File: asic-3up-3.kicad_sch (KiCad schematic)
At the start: 77 parts, among them J10 Conn_01x01, J11 Conn_01x01, U66 MCP1824T-1202E/OT, U67 MCP1824T-1202E/OT, U68 MCP1824T-1202E/OT, U69 MCP1824T-0802E, U70 MCP1824T-0802E, U71 MCP1824T-0802E, U72 BM1362AC_MODE1, U73 BM1362AC_MODE0, U74 BM1362AC_MODE1

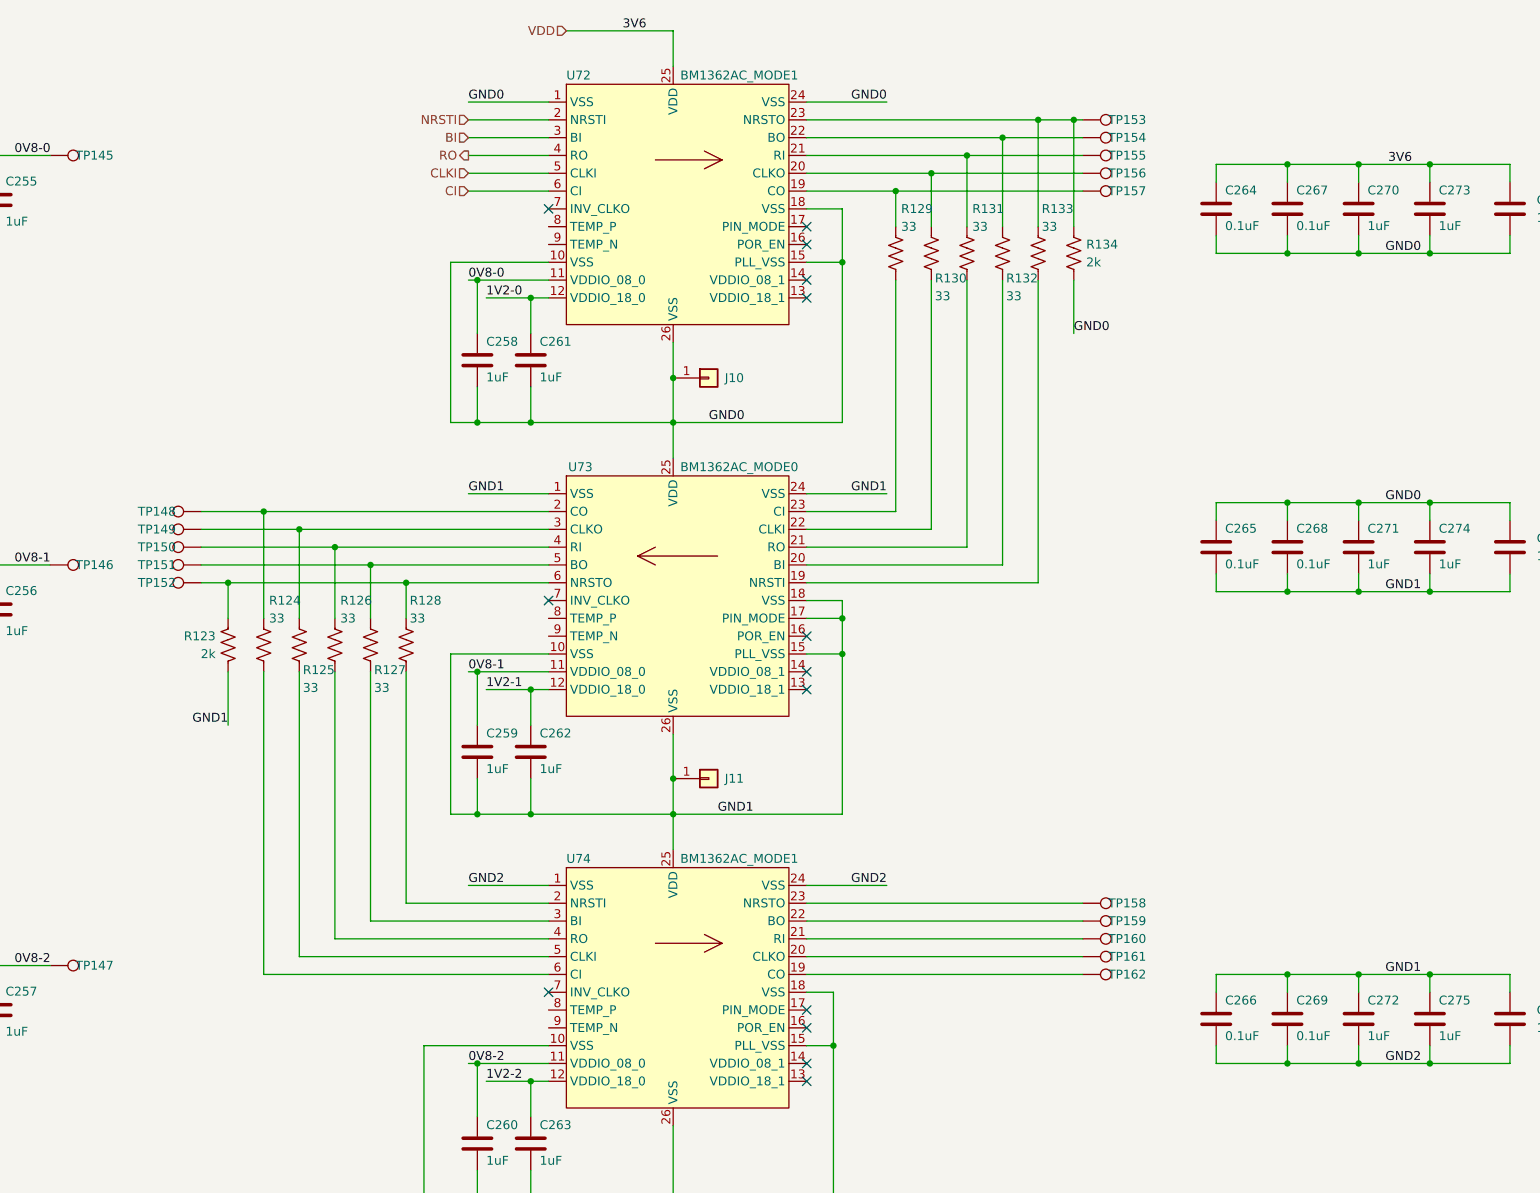
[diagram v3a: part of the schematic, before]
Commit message: so much placing. added mask and paste opening on ASIC footprints. added a pad for a rear heatsink
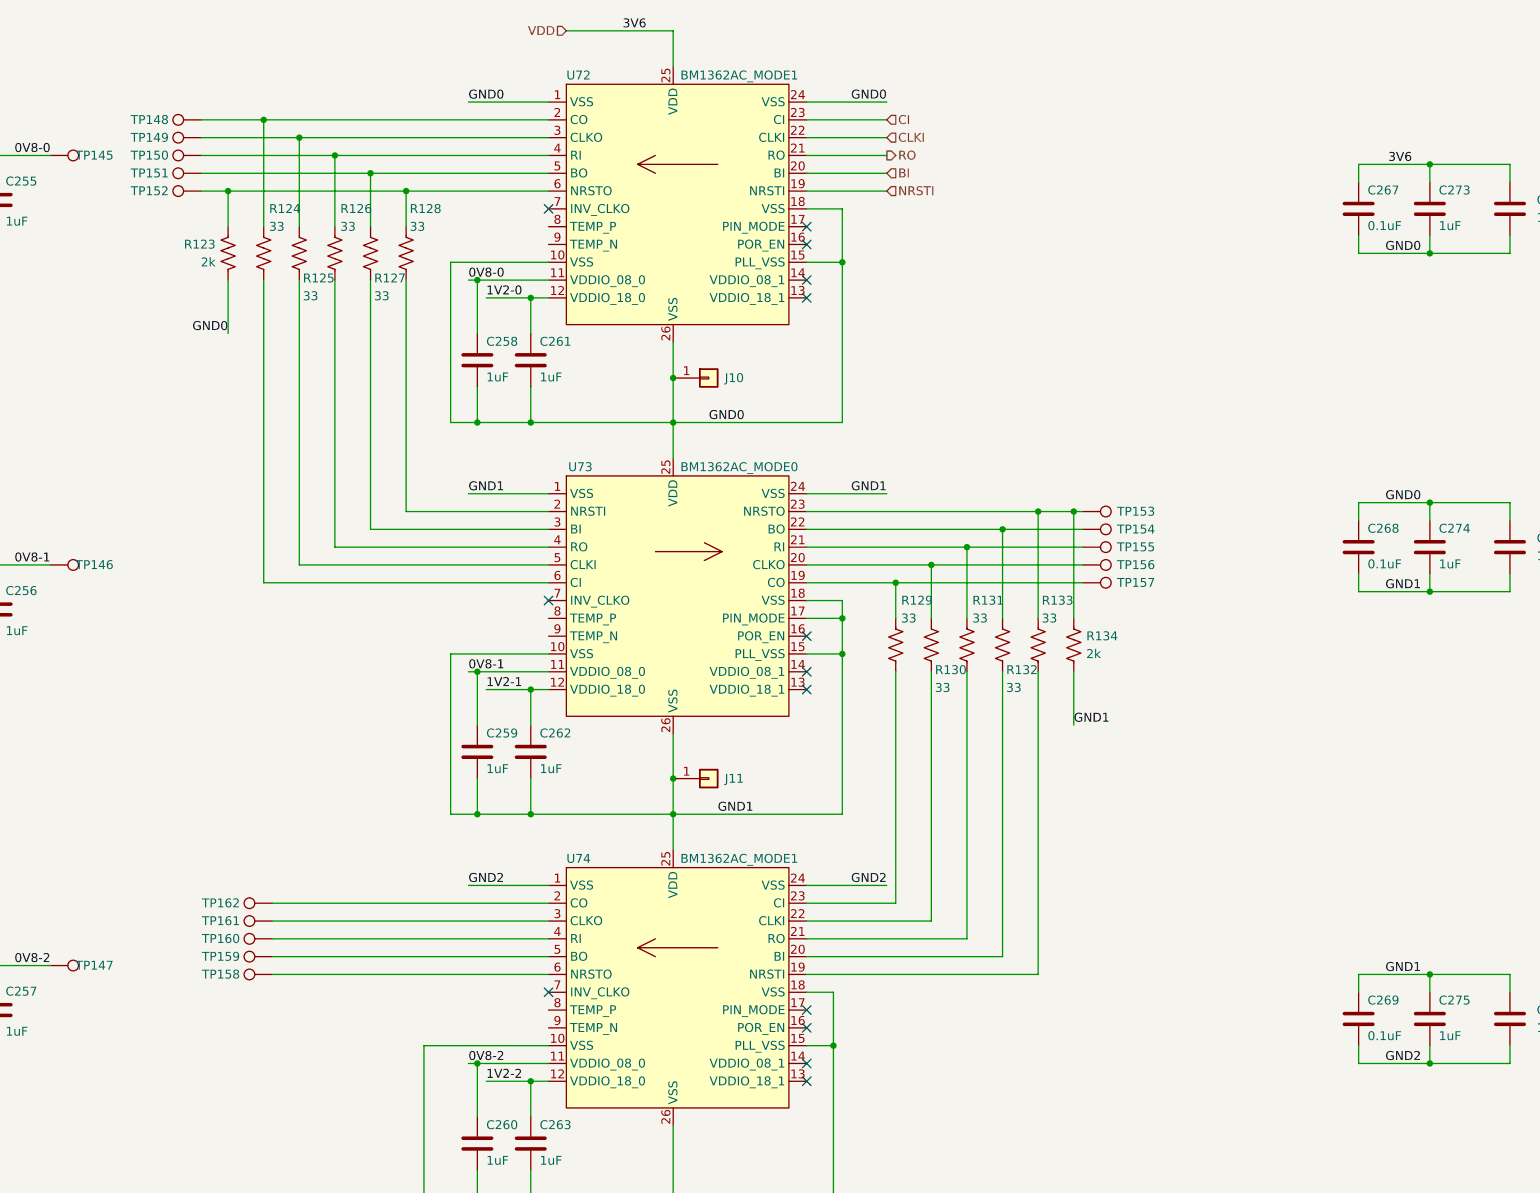
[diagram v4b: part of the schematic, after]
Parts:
- removed C264, C265, C266: 0.1uF, Capacitor_SMD:C_0402_1005Metric, symbol Device:C
- removed C270, C271, C272: 1uF, Capacitor_SMD:C_0402_1005Metric, symbol Device:C
- U72, U74: symbol emberone:BM1362AC_MODE1 -> emberone:BM1362AC_MODE0
- U73: symbol emberone:BM1362AC_MODE0 -> emberone:BM1362AC_MODE1
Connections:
- net BI: now also U72.20 (BI); no longer U72.3 (BI)
- net CI: now also U72.23 (CI); no longer U72.6 (CI)
- net CLKI: now also U72.22 (CLKI); no longer U72.5 (CLKI)
- net GND0: now also R123.2; no longer R134.2
- net GND1: now also R134.2; no longer R123.2
- net NRSTI: now also U72.19 (NRSTI); no longer U72.2 (NRSTI)
- net RO: now also U72.21 (RO); no longer U72.4 (RO)
- net at R133.1, R134.1, TP153.1: now also U73.23 (NRSTO); no longer U72.23 (NRSTO)
- net at R124.1, TP148.1: now also U72.2 (CO); no longer U73.2 (CO)
- net at R130.1, TP156.1: now also U73.20 (CLKO); no longer U72.20 (CLKO)
- net at R130.2: now also U74.22 (CLKI); no longer U73.22 (CLKI)
- net at R129.1, TP157.1: now also U73.19 (CO); no longer U72.19 (CO)
- net at R133.2: now also U74.19 (NRSTI); no longer U73.19 (NRSTI)
- net at TP158.1: now also U74.6 (NRSTO); no longer U74.23 (NRSTO)
- net at R123.1, R128.1, TP152.1: now also U72.6 (NRSTO); no longer U73.6 (NRSTO)
- net at R128.2: now also U73.2 (NRSTI); no longer U74.2 (NRSTI)
- net at R132.1, TP154.1: now also U73.22 (BO); no longer U72.22 (BO)
- net at R131.1, TP155.1: now also U73.21 (RI); no longer U72.21 (RI)
- net at TP160.1: now also U74.4 (RI); no longer U74.21 (RI)
- net at TP161.1: now also U74.3 (CLKO); no longer U74.20 (CLKO)
- net at TP159.1: now also U74.5 (BO); no longer U74.22 (BO)
- net at R132.2: now also U74.20 (BI); no longer U73.20 (BI)
- net at R131.2: now also U74.21 (RO); no longer U73.21 (RO)
- net at R129.2: now also U74.23 (CI); no longer U73.23 (CI)
- net at R125.1, TP149.1: now also U72.3 (CLKO); no longer U73.3 (CLKO)
- net at R126.1, TP150.1: now also U72.4 (RI); no longer U73.4 (RI)
- net at R127.1, TP151.1: now also U72.5 (BO); no longer U73.5 (BO)
- net at TP162.1: now also U74.2 (CO); no longer U74.19 (CO)
- net at R127.2: now also U73.3 (BI); no longer U74.3 (BI)
- net at R126.2: now also U73.4 (RO); no longer U74.4 (RO)
- net at R125.2: now also U73.5 (CLKI); no longer U74.5 (CLKI)
- net at R124.2: now also U73.6 (CI); no longer U74.6 (CI)
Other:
- moved on the sheet: C267, C268, C269, R123, R124, R125, R126, R127, R128, R129, R130, R131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

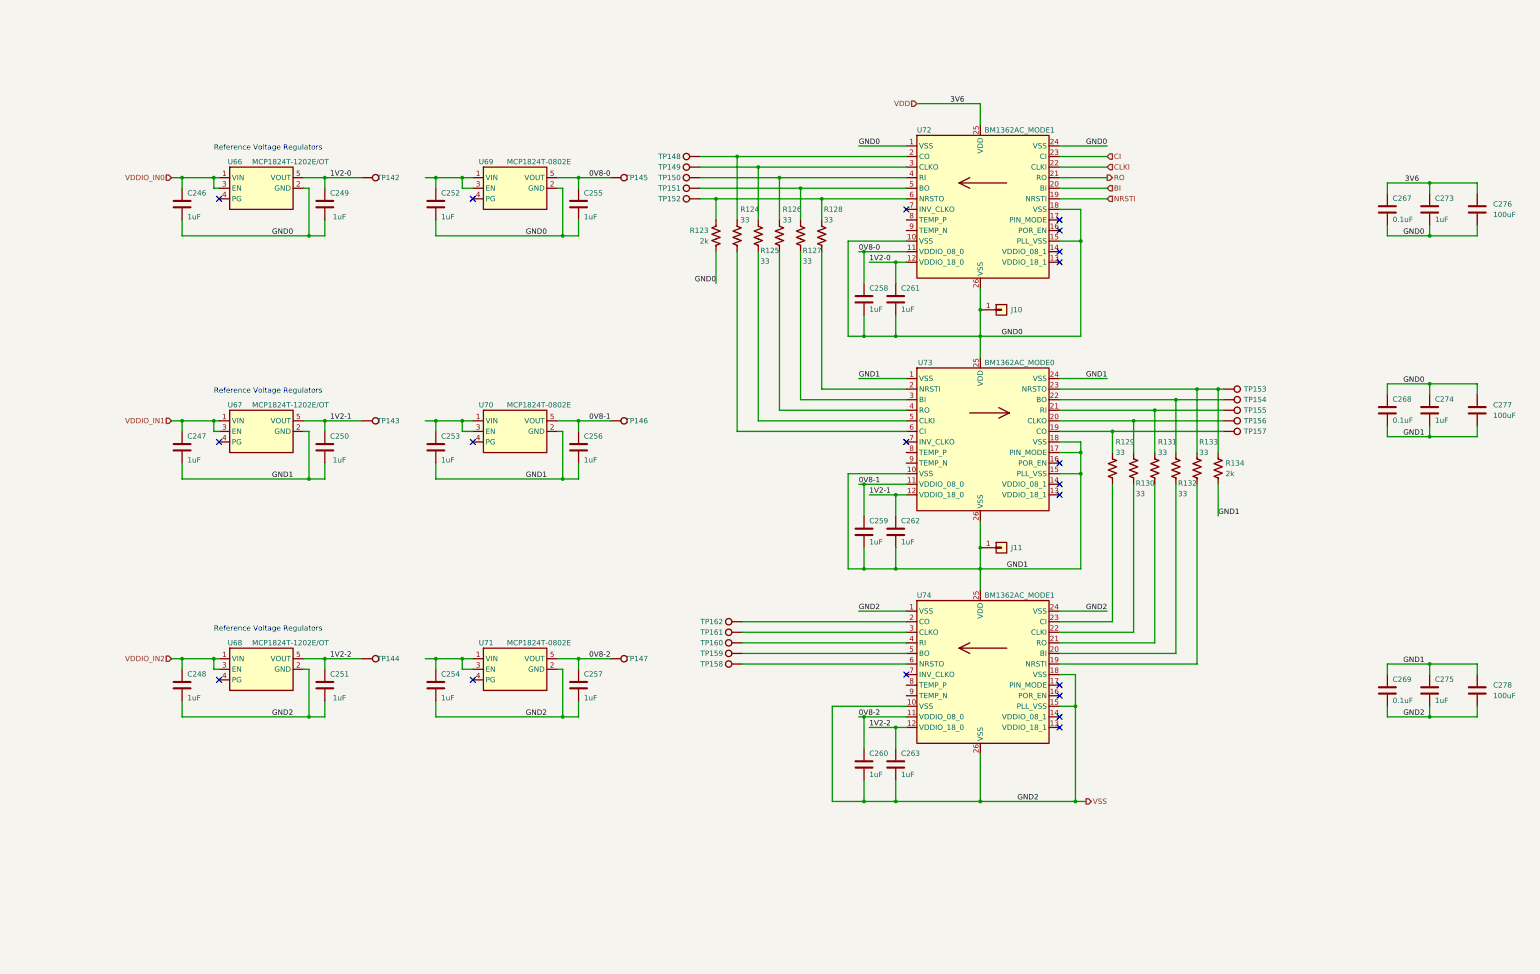
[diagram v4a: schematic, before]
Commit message: forgot that data needs to start with the ASIC that has GND at system GND... reversed everything
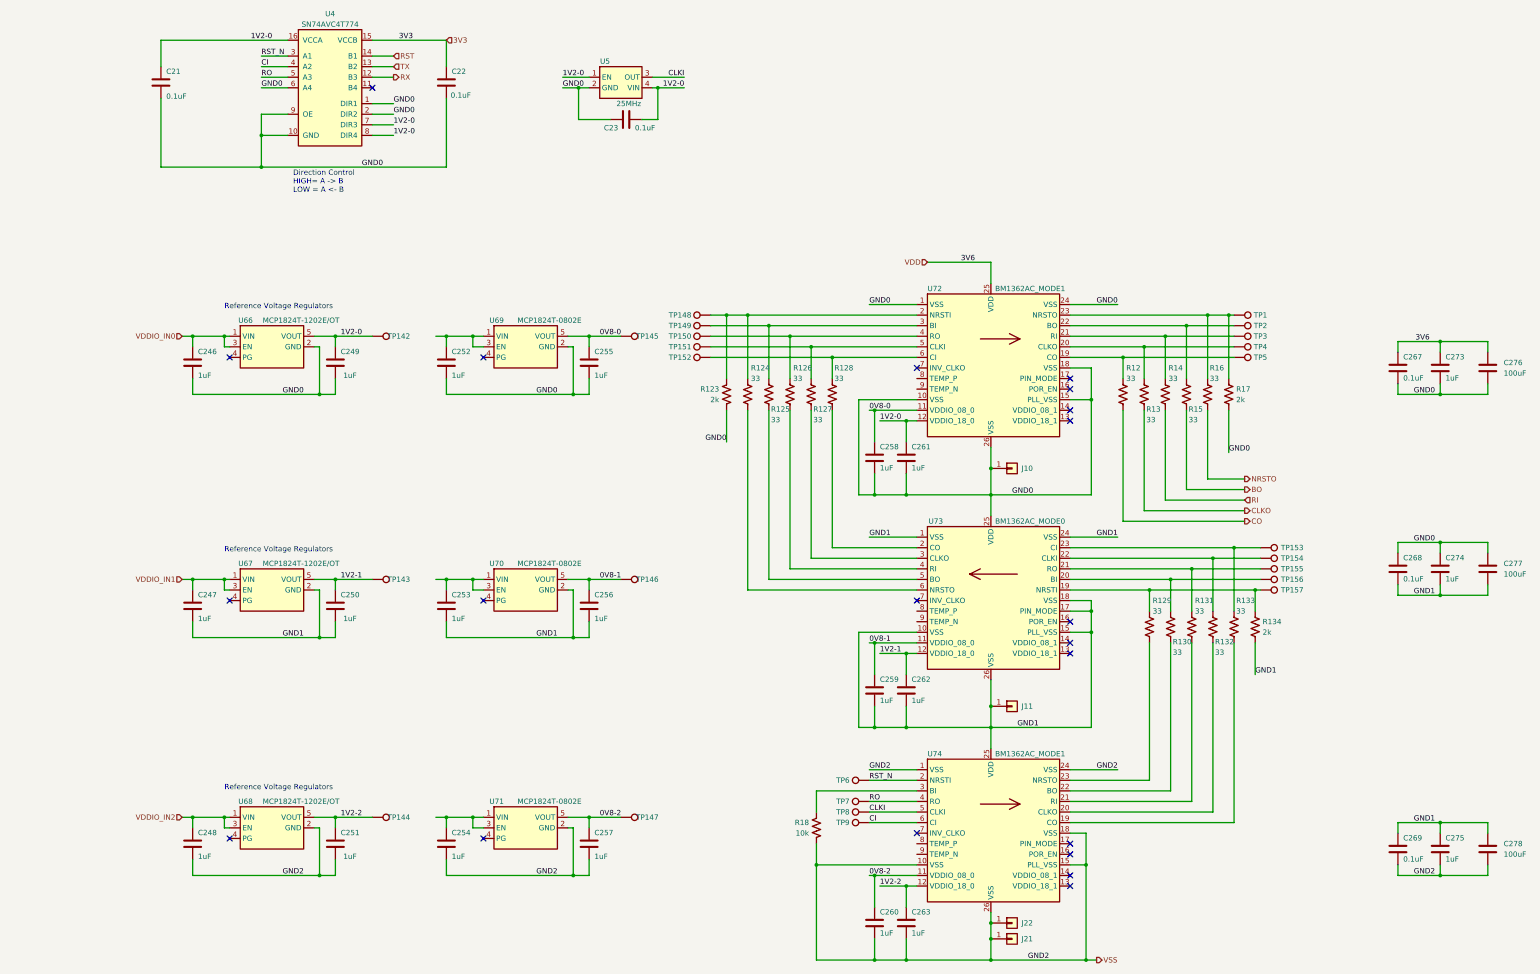
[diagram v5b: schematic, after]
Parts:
- removed TP158, TP159, TP160, TP161, TP162: TestPoint, TestPoint:TestPoint_Pad_D1.5mm, symbol Connector:TestPoint
- added C21, C22, C23: 0.1uF, Capacitor_SMD:C_0402_1005Metric, symbol Device:C
- added J21: Conn_01x01, emberone:5x9_powertab, symbol Connector_Generic:Conn_01x01
- added J22: Conn_01x01, emberone:14x9_powertab_L, symbol Connector_Generic:Conn_01x01
- added R12, R13, R14, R15, R16: 33, Resistor_SMD:R_0402_1005Metric, symbol Device:R_US
- added R17: 2k, Resistor_SMD:R_0402_1005Metric, symbol Device:R_US
- added R18: 10k, Resistor_SMD:R_0402_1005Metric, symbol Device:R_US
- added TP1, TP2, TP3, TP4, TP5, TP6, TP7, TP8, TP9: TestPoint, TestPoint:TestPoint_Pad_D1.5mm, symbol Connector:TestPoint
- added U4: SN74AVC4T774, Package_SO:TSSOP-16_4.4x5mm_P0.65mm, symbol bitaxe:SN74AVC4T774
- added U5: 25MHz, bitaxe:SMD3225-4P, symbol bitaxe:oscillator
- U72, U74: symbol emberone:BM1362AC_MODE0 -> emberone:BM1362AC_MODE1
- U73: symbol emberone:BM1362AC_MODE1 -> emberone:BM1362AC_MODE0
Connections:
- net 1V2-0: now also C21.1, C23.2, U4.16 (VCCA), U4.7 (DIR3), U4.8 (DIR4), U5.1 (EN), U5.4 (VIN)
- net CI: now also U74.6 (CI), TP9.1, U4.4 (A2); no longer U72.23 (CI)
- net CLKI: now also U74.5 (CLKI), TP8.1, U5.3 (OUT); no longer U72.22 (CLKI)
- net GND0: now also C21.2, C22.2, C23.1, R17.2, U4.1 (DIR1), U4.10 (GND), U4.2 (DIR2), U4.6 (A4), U4.9 (OE), U5.2 (GND)
- net RO: now also U74.4 (RO), TP7.1, U4.5 (A3); no longer U72.21 (RO)
- net VSS: now also J21.1 (Pin_1), J22.1 (Pin_1), R18.2
- net at R133.1, TP153.1, U73.23 (CI): no longer R134.1
- net at R124.1, TP148.1, U72.2 (NRSTI): now also R123.1
- net at R129.1, TP157.1, U73.19 (NRSTI): now also R134.1
- net at R128.1, TP152.1, U72.6 (CI): no longer R123.1
- net at U74.3 (BI): now also R18.1
- net RST_N: now reaches U74.2 (NRSTI)
- net RST_N: now also TP6.1, U4.3 (A1)
- net BI: no longer names the net of U72.20 (CLKO)
- net BI: now also R13.1, TP4.1
- net NRSTI: no longer names the net of U72.19 (CO)
- net NRSTI: now also R12.1, TP5.1
- new net: R14.1, TP3.1, U72.21 (RI)
- new net: R16.1, R17.1, TP1.1, U72.23 (NRSTO)
- new net: R15.1, TP2.1, U72.22 (BO)
- new net 3V3: C22.1, U4.15 (VCCB)
- new net BO: R15.2
- new net CLKO: R13.2
- new net CO: R12.2
- new net NRSTO: R16.2
- new net RI: R14.2
- new net RST: U4.14 (B1)
- new net RX: U4.12 (B3)
- new net TX: U4.13 (B2)
- no-connect marks 20 -> 21
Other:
- note added: "Direction Control HIGH= A -> B LOW = A <- B"
- moved on the sheet: C246, C247, C248, C249, C250, C251, C252, C253, C254, C255, C256, C257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

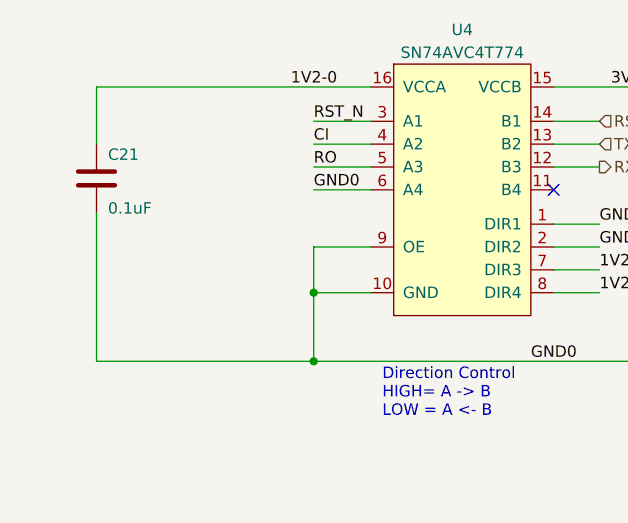
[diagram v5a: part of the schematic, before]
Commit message: added the heatsink mounting holes
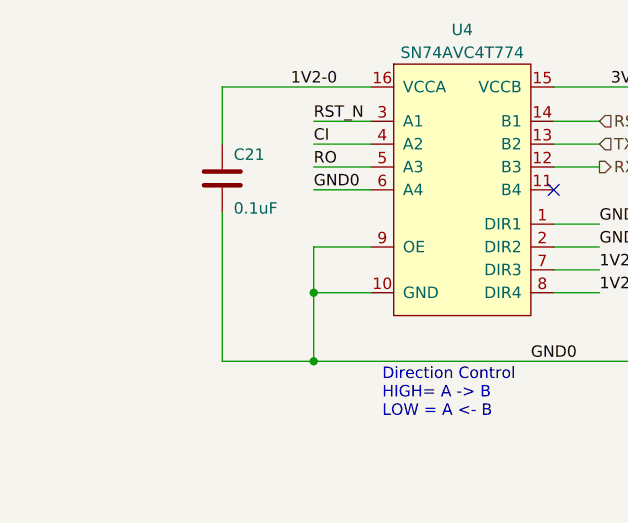
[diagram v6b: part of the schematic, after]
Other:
- moved on the sheet: C21
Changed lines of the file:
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@@
 	(wire
 		(pts
-			(xy 49.53 34.29) (xy 49.53 40.64)
+			(xy 63.5 34.29) (xy 63.5 40.64)
 		)
 		(stroke
@@
 	(wire
 		(pts
-			(xy 49.53 64.77) (xy 73.66 64.77)
+			(xy 63.5 64.77) (xy 73.66 64.77)
 		)
 		(stroke
@@
 	(wire
 		(pts
-			(xy 49.53 48.26) (xy 49.53 64.77)
+			(xy 63.5 48.26) (xy 63.5 64.77)
 		)
 		(stroke
@@
 	(wire
 		(pts
-			(xy 49.53 34.29) (xy 80.01 34.29)
+			(xy 63.5 34.29) (xy 80.01 34.29)
 		)
 		(stroke
@@
 	(symbol
 		(lib_id "Device:C")
-		(at 49.53 44.45 0)
+		(at 63.5 44.45 0)
 		(unit 1)
 		(exclude_from_sim no)
@@
 		(dnp no)
 		(property "Reference" "C21"
-			(at 50.8 42.545 0)
+			(at 64.77 42.545 0)
 			(effects
 				(font
@@
 		)
 		(property "Value" "0.1uF"
-			(at 50.8 48.514 0)
+			(at 64.77 48.514 0)
 			(effects
 				(font
@@
 		)
 		(property "Footprint" "Capacitor_SMD:C_0402_1005Metric"
-			(at 49.53 44.45 0)
+			(at 63.5 44.45 0)
 			(effects
 				(font
@@
 		)
 		(property "Datasheet" ""
-			(at 49.53 44.45 0)
+			(at 63.5 44.45 0)
 			(effects
 				(font
@@
 		)
 		(property "Description" ""
-			(at 49.53 44.45 0)
+			(at 63.5 44.45 0)
 			(effects
 				(font
@@
 		)
 		(property "DK" "1276-1234-1-ND"
-			(at 49.53 44.45 0)
+			(at 63.5 44.45 0)
 			(effects
 				(font
@@
 		)
 		(property "PARTNO" "CL05A104KO5NNNC"
-			(at 49.53 44.45 0)
+			(at 63.5 44.45 0)
 			(effects
 				(font
